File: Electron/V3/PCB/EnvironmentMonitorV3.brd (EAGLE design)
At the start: 92.7 x 31.8 mm, 16 parts, among them U1 HTU21DSMD, U2 BMP180, U4 LIGHTSENSORTEMT6000

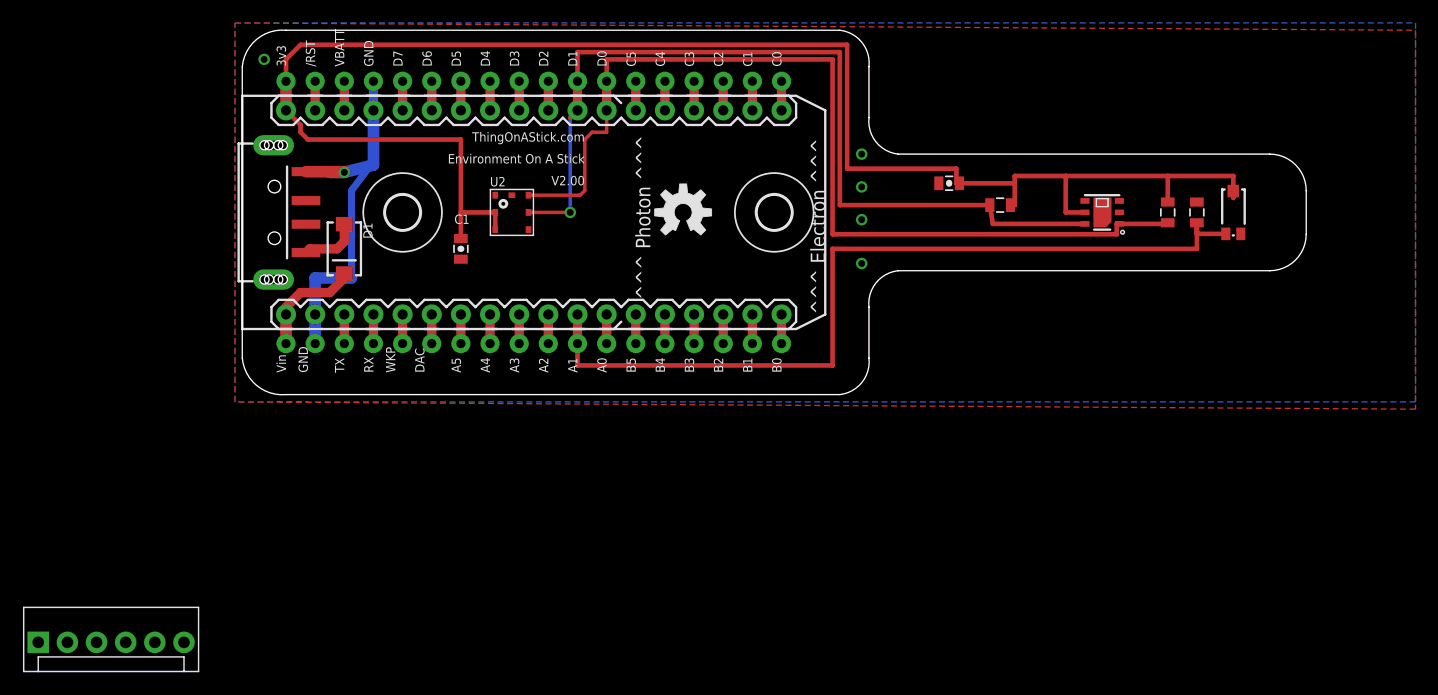
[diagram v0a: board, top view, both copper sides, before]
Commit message: Added BME680 to V3 and removed other sensors (except light).
Added images for V2 and V3 PCBs.

PCBs sent to DirtyPCB for fab.
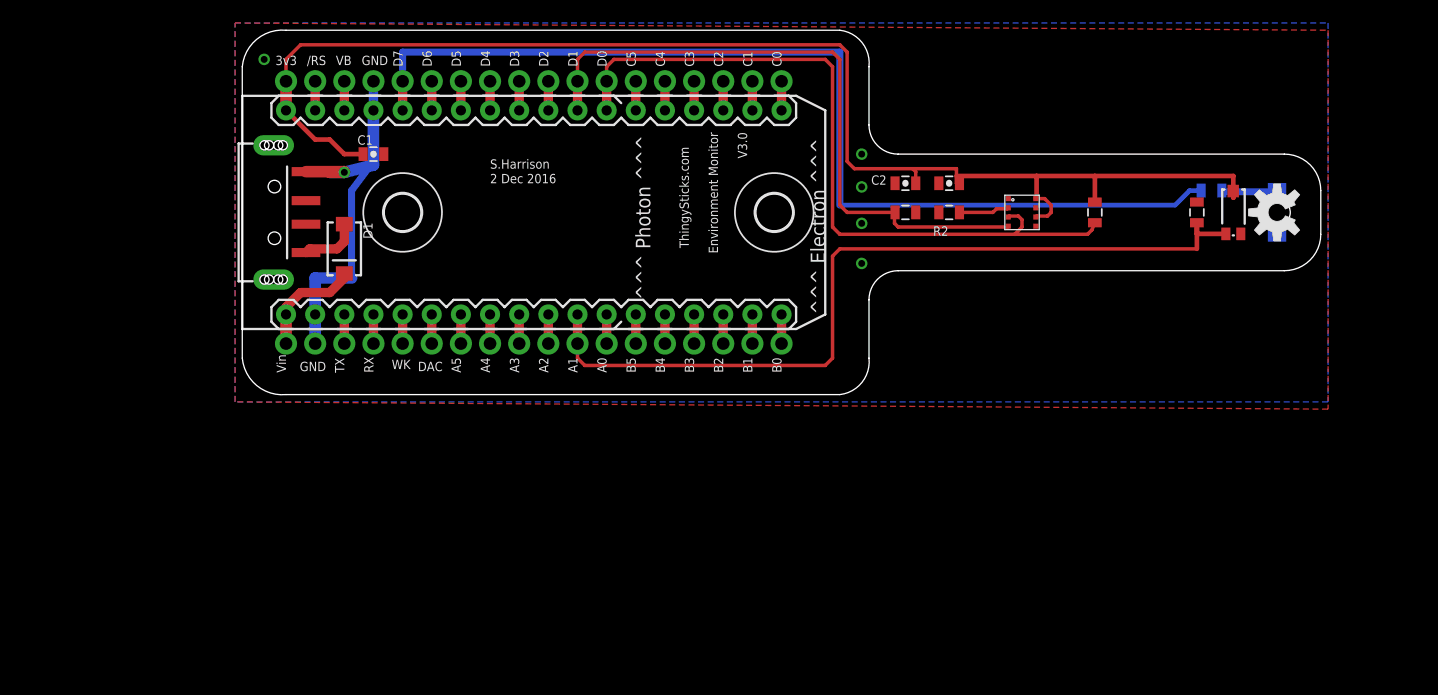
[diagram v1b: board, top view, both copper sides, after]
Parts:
- removed JP2: (no value), SparkFun-Connectors:MOLEX-1X6
- removed U1: HTU21DSMD, SparkFun-Sensors:HTU21D
- removed U2: BMP180, SparkFun-Sensors:BMP180
- added C2: 0.1uF, SparkFun-Capacitors:0805-CAP
- added D2: (no value), SparkFun-LED:LED-1206-BOTTOM
- added IC1: BME680, bosch-bme680:BME680
- added R1: 310R, SparkFun-Resistors:0805
- added R2: 0R, SparkFun-Resistors:0805
- H1, H2: value MOUNT-HOLE3.0 -> MOUNT-HOLE3.2; device holes:3,0 -> holes:3,2
- moved LOGO1 51.8 mm to (90.2, 15.9), turned to 90 degrees
- moved C1 11.2 mm to (11.4, 21.0), turned to 180 degrees
- moved R4 8.28 mm to (57.8, 15.9)
- moved R3 6.35 mm to (74.3, 15.9)
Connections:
- new net N$6: D2.A, R1.1
- new net OSHLED: R1.2, U$1.D7, U$1.D7_1
- net 3.3V: now also C2.2, IC1.6, IC1.8; no longer U1.VDD, U2.2, U2.3
- net GND: now also C2.1, D2.C, IC1.1, IC1.7, R2.2; no longer U1.7, U1.GND, U2.7
- net N$3: now also IC1.2, R2.1; no longer U$1.D7, U$1.D7_1
- net SCL: now also IC1.4; no longer U1.SCK, U2.5
- net SDA: now also IC1.3; no longer U1.DATA, U2.6
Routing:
- net OSHLED: track 0.00 -> 88.5 mm
- net 3.3V: track 141.9 -> 119.3 mm
- net SCL: track 77.7 -> 56.7 mm, vias 1 -> 0
- net SDA: track 83.2 -> 64.7 mm
- net N$6: track 0.00 -> 4.92 mm
- net N$3: track 2.54 -> 4.42 mm
- net LIGHTLEVEL_ANALOG: track 74.3 -> 73.2 mm
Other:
- board size 92.7 x 31.8 mm -> 94 x 31.8 mm
- board text added: "2 Dec 2016"
- board text added: "Environment Monitor"
- board text added: "S.Harrison"
- board text added: "ThingySticks.com"
- board text added: "V3.0"
- board text removed: "Environment On A Stick"
- board text removed: "ThingOnAStick.com"
- board text removed: "V2.00"

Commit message: Updated with light sensor and BME680
*** DO NOT USE *** BME680 pads flipped.
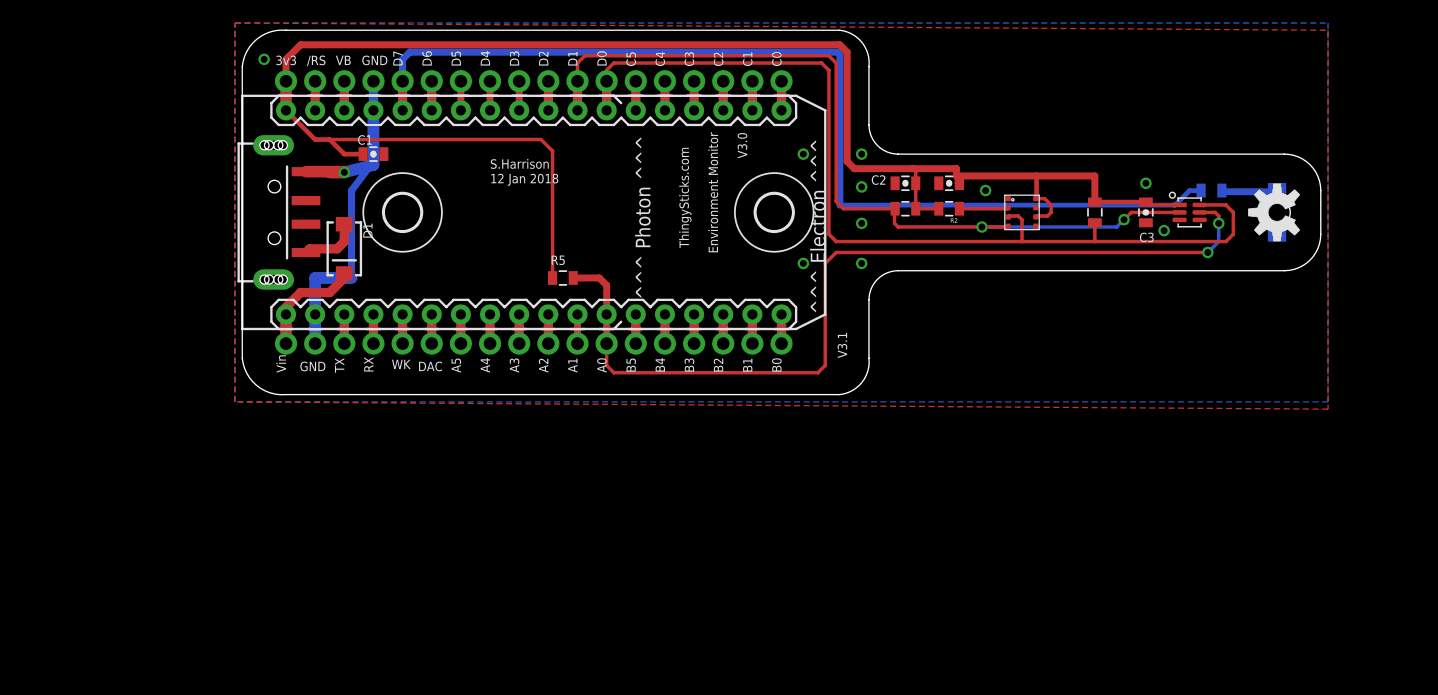
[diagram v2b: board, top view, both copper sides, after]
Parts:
- removed R6: 10k, SparkFun-Resistors:0805
- removed U4: LIGHTSENSORTEMT6000, SparkFun-Sensors:TEMT6000-SEN
- added C3: 0.1uF, SparkFun-Capacitors:0805-CAP
- added R5: 10k, SparkFun-Resistors:0805
- added U$2: TCS3472, TCS3472:FN-6
- R2: value 0R -> 4k7
- moved R2 0.32 mm to (61.6, 16.2)
- moved R4 0.32 mm to (57.8, 16.2)
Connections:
- net 1WIRE-DQ renamed N$7
- net EXTERNAL_INT renamed N$9
- net INT renamed N$10
- removed net LIGHTLEVEL_ANALOG: R6.2, U$1.A1, U$1.A1_1, U4.EMITTER
- removed net UV_LEVEL: U$1.A0, U$1.A0_1
- new net LIGHT_INT: R5.1, U$1.A0, U$1.A0_1, U$2.5
- new net N$23: U$1.A1, U$1.A1_1
- net 3.3V: now also C3.2, R2.2, R5.2, U$2.1; no longer U4.COLLECTOR
- net GND: now also C3.1, IC1.5, U$2.3; no longer R2.2, R6.1
- net SCL: now also U$2.2
- net SDA: now also U$2.6
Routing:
- net LIGHT_INT: track 0.00 -> 77.7 mm, vias 0 -> 2
- net LIGHTLEVEL_ANALOG: track 73.2 -> 0.00 mm
- net 3.3V: track 119.3 -> 147.4 mm
- net SDA: track 64.7 -> 83.6 mm
- net SCL: track 56.7 -> 73.8 mm, vias 0 -> 2
- net UV_LEVEL: track 2.54 -> 0.00 mm
- net N$23: track 0.00 -> 2.54 mm
- net GND: vias 6 -> 11
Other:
- board text added: "12 Jan 2018"
- board text added: "V3.1"
- board text removed: "2 Dec 2016"
